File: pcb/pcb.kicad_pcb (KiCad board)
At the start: 2 copper layers, 48 x 60 mm, 51 parts, among them J1 USB_C_Receptacle_USB2.0_14P, J2 LCD, J4 LCD CTRL, J5 Moisture, J6 HC-05, J7 DEBUG, J9 USART3 TX, SW1 PWR SWITCH, U1 TLV62569DBV, U2 STM32F446RETx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

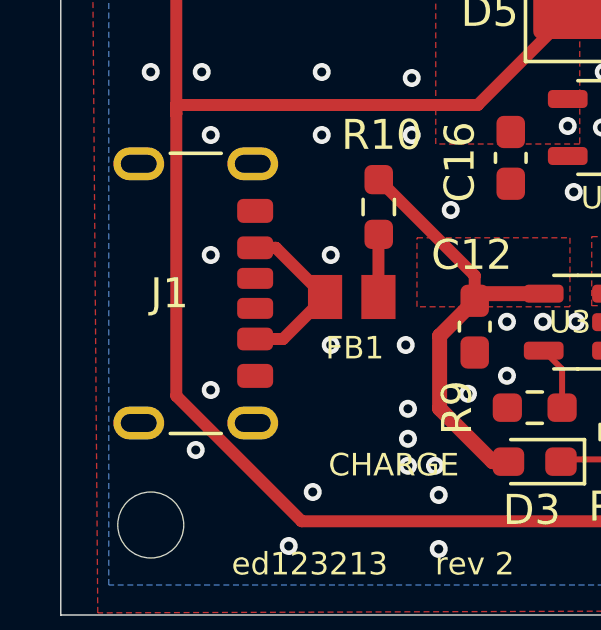
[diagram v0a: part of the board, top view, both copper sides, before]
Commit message: Add more vias
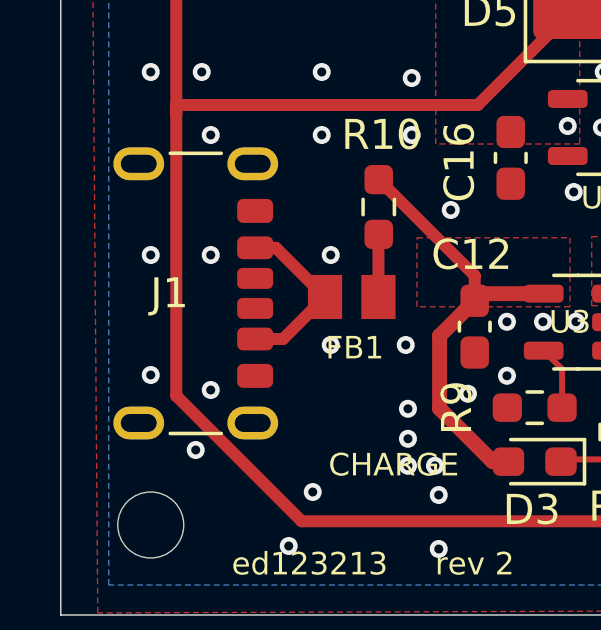
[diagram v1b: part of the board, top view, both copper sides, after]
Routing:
- net GND: vias 192 -> 194
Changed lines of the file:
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@@
+	)
+	(via
+		(at 67 87.5)
+		(size 0.6)
+		(drill 0.3)
+		(layers "F.Cu" "B.Cu")
+		(free yes)
+		(net 1)
 	)
 	(via
@@
 		(size 0.6)
 		(drill 0.3)
+		(layers "F.Cu" "B.Cu")
+		(free yes)
+		(net 1)
+	)
+	(via
+		(at 67 91.5)
+		(size 0.6)
+		(drill 0.3)

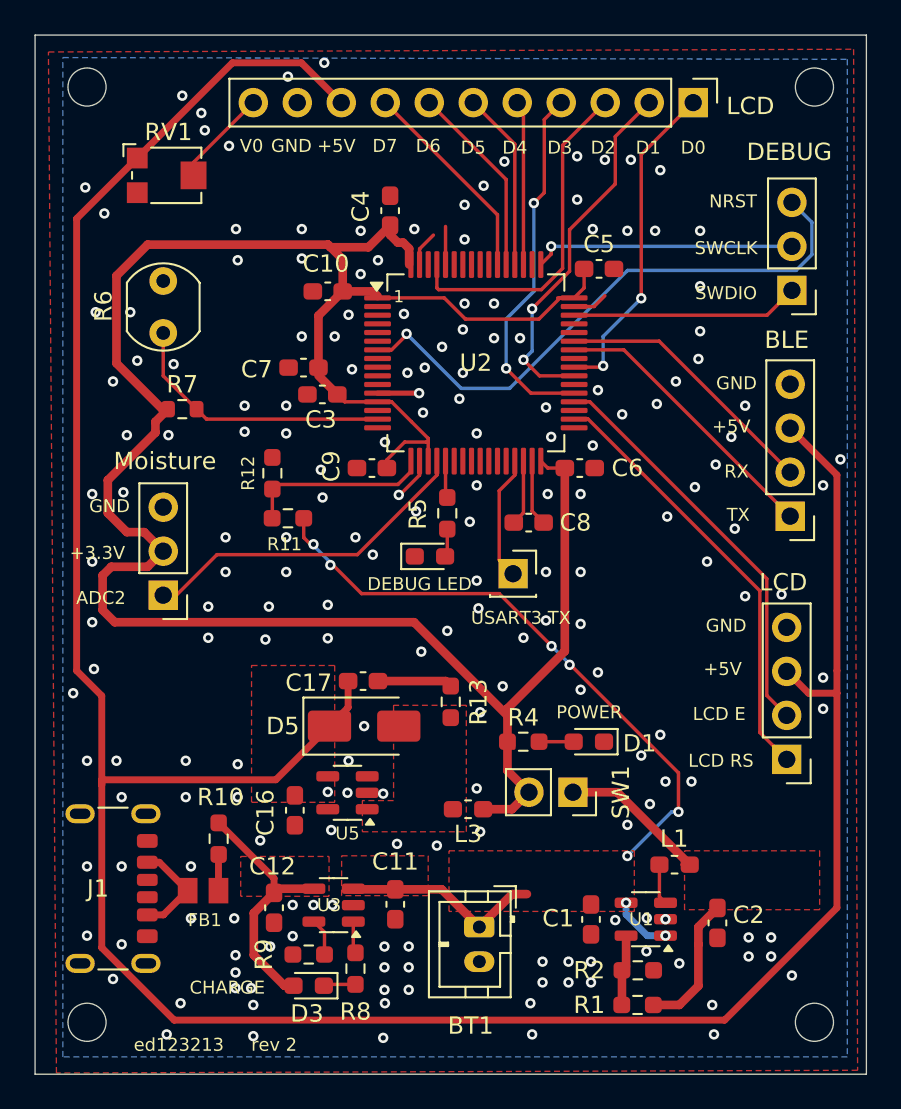
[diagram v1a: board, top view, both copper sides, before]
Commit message: Add more vias and input capacitor to schematic
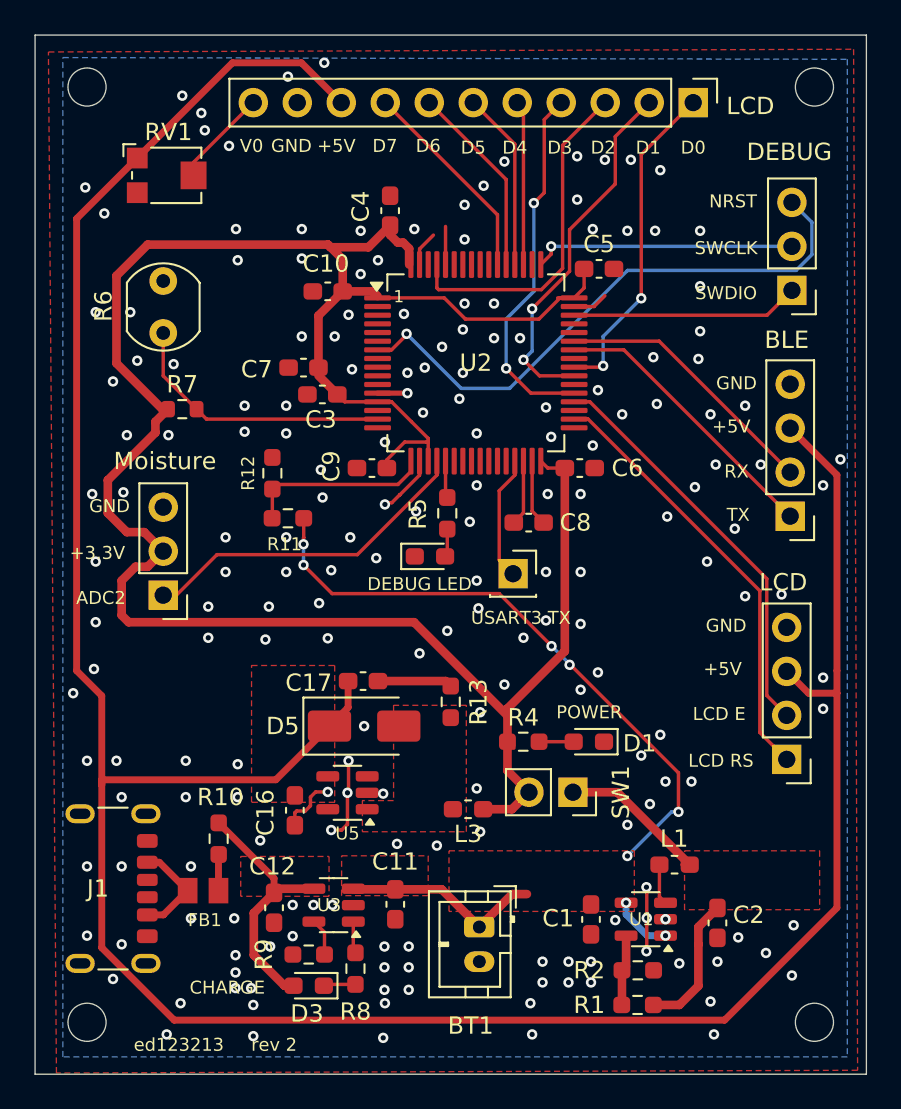
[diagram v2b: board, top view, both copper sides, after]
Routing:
- net GND: track 15.2 -> 27.4 mm, vias 194 -> 197
- net +3.3V: track 137.1 -> 134.9 mm
- net +Vbat: track 50.2 -> 51.1 mm

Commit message: add input capacitor to boost converter
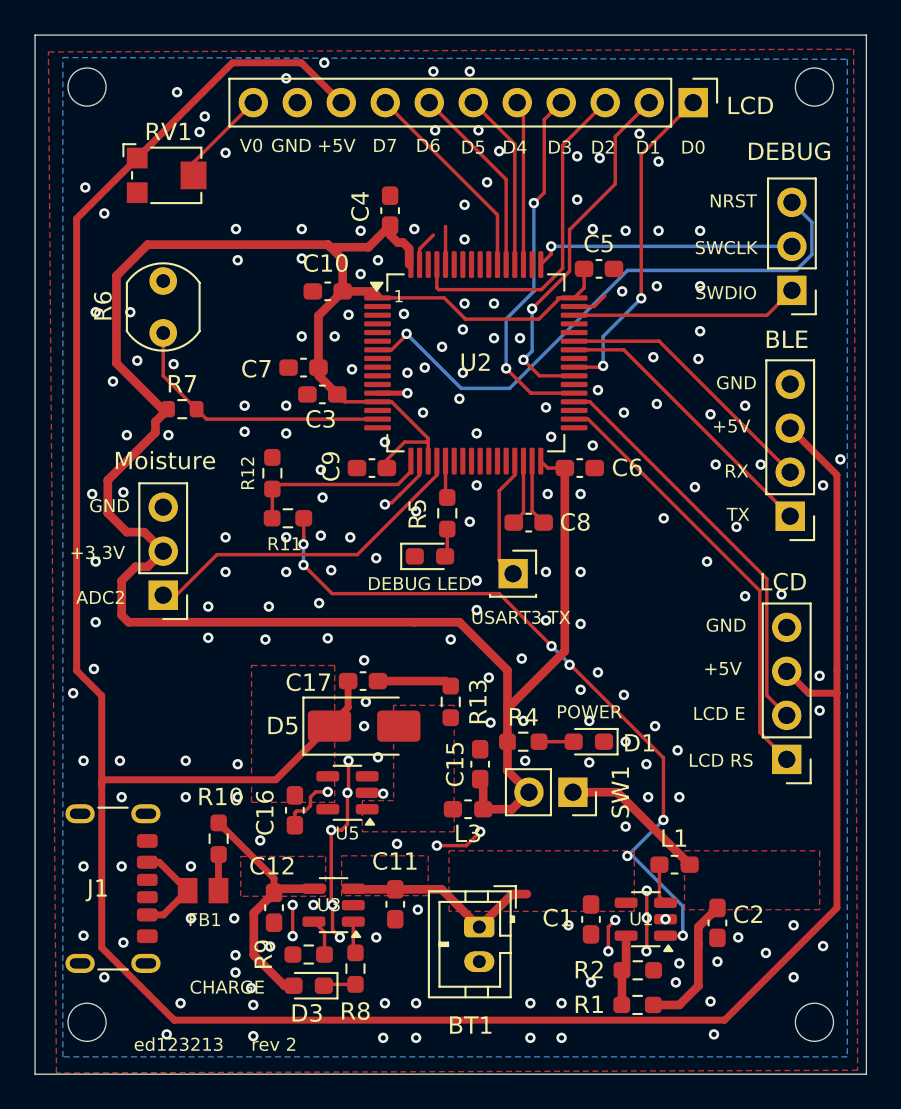
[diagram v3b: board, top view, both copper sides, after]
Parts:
- added C15: 10uF, Capacitor_SMD:C_0603_1608Metric_Pad1.08x0.95mm_HandSolder, F.Cu at (89.7, 81.6)
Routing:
- net GND: track 27.4 -> 40.0 mm, vias 197 -> 210
- net +3.3V: track 134.9 -> 137.8 mm
- net +Vbat: track 51.1 -> 54.0 mm, vias 8 -> 7

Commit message: Add volgo bluetooth module to pcb
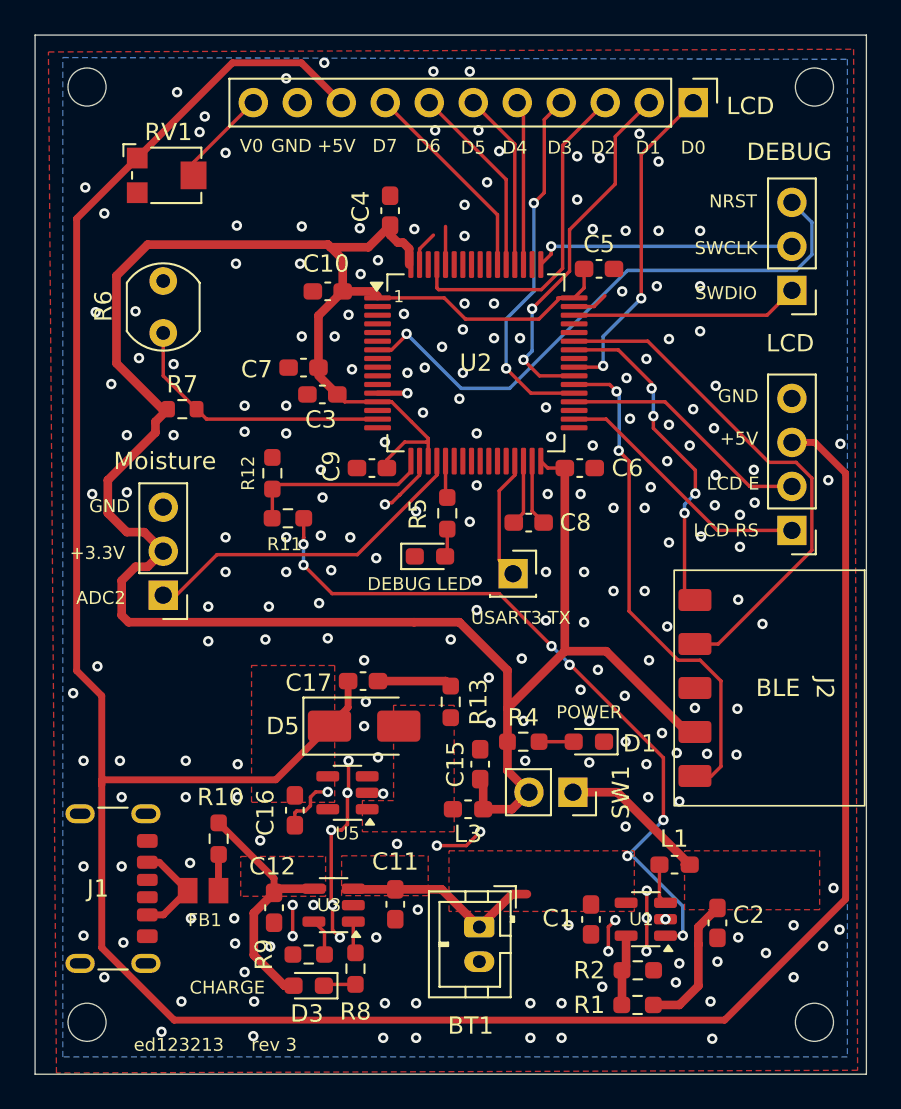
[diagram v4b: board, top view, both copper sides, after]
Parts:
- removed J6: HC-05, Connector_PinHeader_2.54mm:PinHeader_1x04_P2.54mm_Vertical
- added J2: VG6328A, custom:Vollgo VG6328A, F.Cu at (110.9, 77.2)
- moved J4 13.2 mm to (107.7, 68.1)
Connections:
- U2 pad 38: unconnected-(U2-PC7-Pad38) -> BT CONNECT
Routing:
- net BT CONNECT: track 0.00 -> 29.3 mm, vias 0 -> 2
- net USART1 RX: track 15.6 -> 29.4 mm
- net LCD RS: track 25.2 -> 15.2 mm
- net +3.3V: track 137.8 -> 147.3 mm
- net LCD E: track 23.7 -> 14.6 mm
- net +5V: track 159.5 -> 156.4 mm
- net USART1 TX: track 16.5 -> 19.3 mm, vias 0 -> 4
- net GND: vias 210 -> 223
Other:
- board text added: "rev 3"
- board text removed: "RX"
- board text removed: "TX"
- board text removed: "rev 2"

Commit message: Improve volgo bluetooth footprint and add pull up for bt connect pin
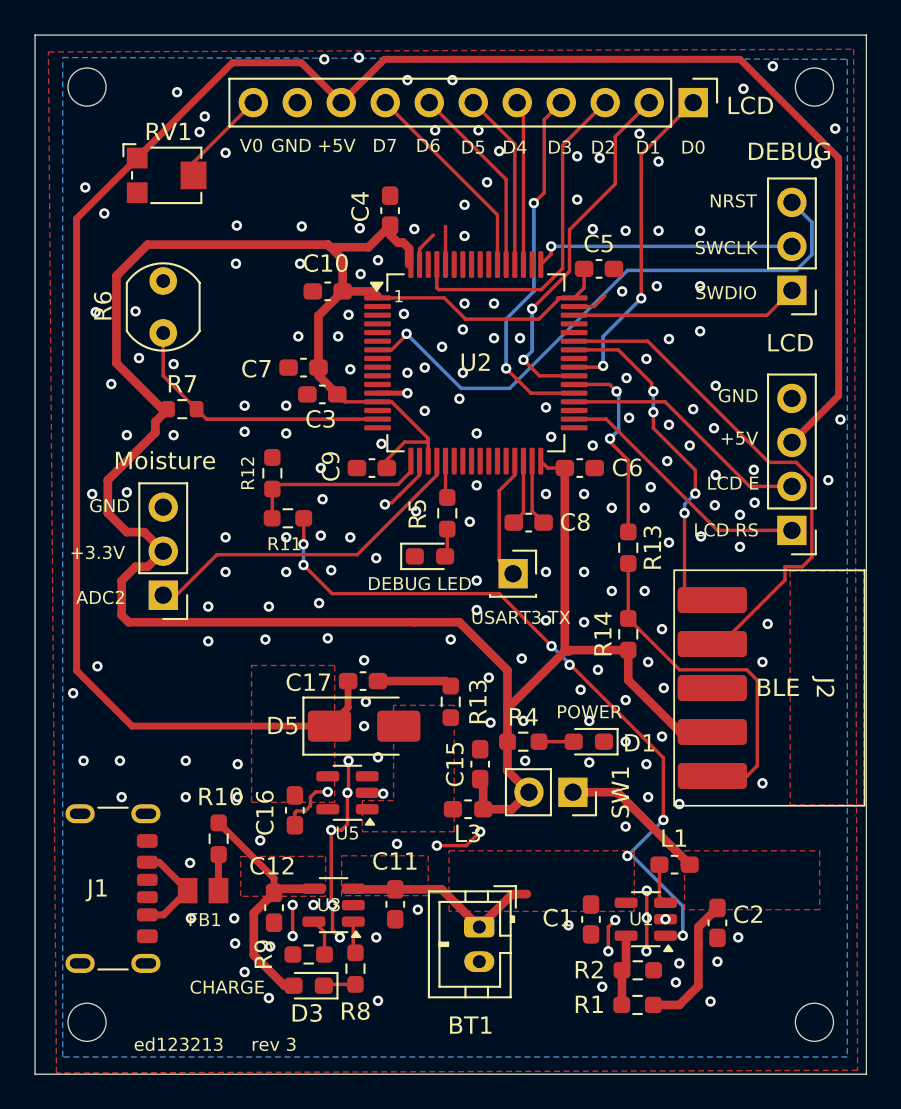
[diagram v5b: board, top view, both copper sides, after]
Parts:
- added R13: 1k, Resistor_SMD:R_0603_1608Metric_Pad0.98x0.95mm_HandSolder, F.Cu at (98.2, 69.1)
- added R14: 100k, Resistor_SMD:R_0603_1608Metric_Pad0.98x0.95mm_HandSolder, F.Cu at (98.2, 74.1)
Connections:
- J2 pad 5: BT CONNECT -> Net-(J2-Pin_5)
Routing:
- net +5V: track 156.4 -> 114.7 mm
- net Net-(J2-Pin_5): track 0.00 -> 21.6 mm
- net BT CONNECT: track 29.3 -> 11.4 mm
- net +3.3V: track 147.3 -> 149.8 mm
- net USART1 RX: track 29.4 -> 31.4 mm
- net GND: vias 223 -> 202
- added copper zone on F.Cu, net (none)

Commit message: case v3
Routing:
- net GND: vias 202 -> 209
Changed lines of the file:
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@@
 	)
 	(gr_text "1"
-		(at 85 54.6 0)
+		(at 83.7 53.2 0)
 		(layer "F.SilkS")
 		(effects
@@
 	)
 	(via
-		(at 75.7 81.6)
+		(at 75.7 80.5)
+		(size 0.6)
+		(drill 0.3)
+		(layers "F.Cu" "B.Cu")
+		(free yes)
+		(net 1)
+	)
+	(via
+		(at 102.4 70.5)
 		(size 0.6)
 		(drill 0.3)
@@
 	)
 	(via
-		(at 66.9 48.3)
+		(at 66.8 48.2)
 		(size 0.6)
 		(drill 0.3)
@@
 	)
 	(via
-		(at 68 49.8)
+		(at 68.1 49.9)
 		(size 0.6)
 		(drill 0.3)
@@
 	)
 	(via
+		(at 100.5 70.6)
+		(size 0.6)
+		(drill 0.3)
+		(layers "F.Cu" "B.Cu")
+		(free yes)
+		(net 1)
+	)
+	(via
 		(at 86.5 58.7)
 		(size 0.6)
@@
 	)
 	(via
+		(at 72.8 78.3)
+		(size 0.6)
+		(drill 0.3)
+		(layers "F.Cu" "B.Cu")
+		(free yes)
+		(net 1)
+	)
+	(via
 		(at 81.6 91.6)
 		(size 0.6)
@@
 	)
 	(via
-		(at 66.8 81.4)
+		(at 67.5 78.9)
 		(size 0.6)
 		(drill 0.3)
@@
 	)
 	(via
+		(at 75.7 78.3)
+		(size 0.6)
+		(drill 0.3)
+		(layers "F.Cu" "B.Cu")
+		(free yes)
+		(net 1)
+	)
+	(via
 		(at 87.2 86.3)
 		(size 0.6)
@@
 	)
 	(via
-		(at 72.7 81.4)
+		(at 72.7 80.5)
 		(size 0.6)
 		(drill 0.3)
@@
 	)
 	(via
+		(at 68.9 77.2)
+		(size 0.6)
+		(drill 0.3)
+		(layers "F.Cu" "B.Cu")
+		(free yes)
+		(net 1)
+	)
+	(via
 		(at 90.5 55)
 		(size 0.6)
@@
 	)
 	(via
-		(at 68.9 81.4)
+		(at 69.2 80.5)
 		(size 0.6)
 		(drill 0.3)
@@
 	)
 	(via
+		(at 70 78.3)
+		(size 0.6)
+		(drill 0.3)
+		(layers "F.Cu" "B.Cu")
+		(free yes)
+		(net 1)
+	)
+	(via
 		(at 84.2 66.6)
 		(size 0.6)
@@
 		(size 0.6)
 		(drill 0.3)
+		(layers "F.Cu" "B.Cu")
+		(free yes)
+		(net 1)
+	)
+	(via
+		(at 105.8 71.1)
+		(size 0.6)
+		(drill 0.3)
